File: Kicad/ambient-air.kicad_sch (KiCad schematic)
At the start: 38 parts, among them J1 USB_C_Receptacle_USB2.0_14P, J2 Conn_01x02, SW1 SW_Push, SW2 MINI MSK12CO2, SW3 SW_Push, U1 MCP73831T-2ACI/MC, U2 AP7361C-33SP-13, U3 ESP32-C3-WROOM-02, U4 TPD4E05U06DQA, U5 SHT4x, U6 STCC4-D1, U7 AHT20_C2757850, U8 SGP40-D-R4, U9 ICP-20100

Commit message: Separated PCBs
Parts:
- added C10: 4.7µF, Capacitor_SMD:C_0805_2012Metric, symbol Device:C_Small
- added J3, J4: Conn_01x04, Connector_JST:JST_SH_SM04B-SRSS-TB_1x04-1MP_P1.00mm_Horizontal, symbol Connector_Generic:Conn_01x04
- U7: now fitted
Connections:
- net +3V3: now also J3.1 (Pin_1); no longer C7.1, C8.1, C9.1, R6.2, U5.3 (VDD), U6.3 (ADDR), U6.6 (VDDIO), U6.7 (VDD), U7.2 (VDD), U8.5 (VDDH), U9.1 (CSB), U9.10 (VDDIO), U9.5 (VDD)
- net GND: now also J3.4 (Pin_4); no longer C7.2, C8.2, C9.2, U5.4 (VSS), U6.4 (VSS), U7.5 (GND), U8.2 (VSS), U8.4 (N/A), U8.7 (EXP), U9.3 (VSS), U9.6 (SDO/AD0), U9.8 (RESV), U9.9 (RESV)
- net SCL: now also J3.2 (Pin_2); no longer U6.1 (SCL), U7.3 (SCL), U8.6 (SCL), U9.2 (SCL)
- net SDA: now also J3.3 (Pin_3); no longer U6.5 (SDA), U7.4 (SDA), U8.3 (SDA), U9.4 (SDA/SDIO/SDI)
- new net +3V3_EXT: C10.1, C7.1, C8.1, C9.1, J4.1 (Pin_1), R6.2, U5.3 (VDD), U6.3 (ADDR), U6.6 (VDDIO), U6.7 (VDD), U7.2 (VDD), U8.5 (VDDH), U9.1 (CSB), U9.10 (VDDIO), U9.5 (VDD)
- new net GND_EXT: C10.2, C7.2, C8.2, C9.2, J4.4 (Pin_4), U5.4 (VSS), U6.4 (VSS), U7.5 (GND), U8.2 (VSS), U8.4 (N/A), U8.7 (EXP), U9.3 (VSS), U9.6 (SDO/AD0), U9.8 (RESV), U9.9 (RESV)
- new net SCL_EXT: J4.2 (Pin_2), U6.1 (SCL), U7.3 (SCL), U8.6 (SCL), U9.2 (SCL)
- new net SDA_EXT: J4.3 (Pin_3), U6.5 (SDA), U7.4 (SDA), U8.3 (SDA), U9.4 (SDA/SDIO/SDI)
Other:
- moved on the sheet: C7, C8, C9, J1, J2, JP1, R10, R6, R7, R8, R9, U5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

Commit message: Battery fuel gauge
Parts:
- added C11: 470nF, Capacitor_SMD:C_0805_2012Metric, symbol Device:C_Small
- added C12: 1µF, Capacitor_SMD:C_0805_2012Metric, symbol Device:C_Small
- added R11: 0.01Ω, Resistor_SMD:R_0805_2012Metric, symbol Device:R_Small
- added R12, R13: 10kΩ, Resistor_SMD:R_0805_2012Metric, symbol Device:R_Small
- added U10: BQ27441-G1, Package_SON:Texas_S-PDSO-N12, symbol Battery_Management:BQ27441-G1
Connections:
- net GND: now also C11.2, C12.1, R12.2, U10.13 (PAD), U10.3 (V_{SS})
- net SCL: now also U10.2 (SCL)
- net SDA: now also U10.1 (SDA)
- net VBAT: now also R11.1, U10.7 (SRN); no longer J2.1 (Pin_1)
- new net: R12.1, U10.10 (BIN)
- new net: R13.2, U10.12 (GPOUT)
- new net: C11.1, R13.1, U10.5 (V_{DD})
- new net VBAT_PRE: C12.2, J2.1 (Pin_1), R11.2, U10.6 (BAT), U10.8 (SRP)
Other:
- note added: "I2C Address: 0x55"
- moved on the sheet: C10, C7, C8, C9, J2, J4, R5, R6, U5, U6, U7, U8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

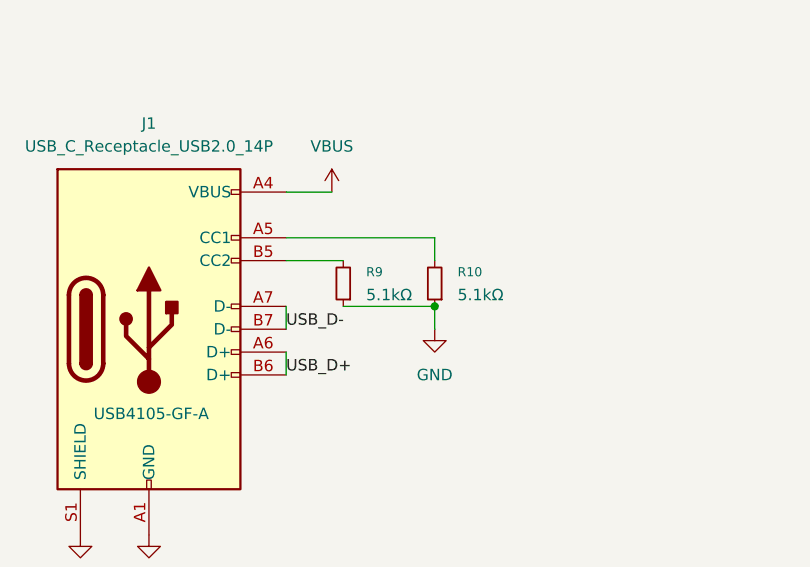
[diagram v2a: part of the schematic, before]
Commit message: Progress, saving data to storage
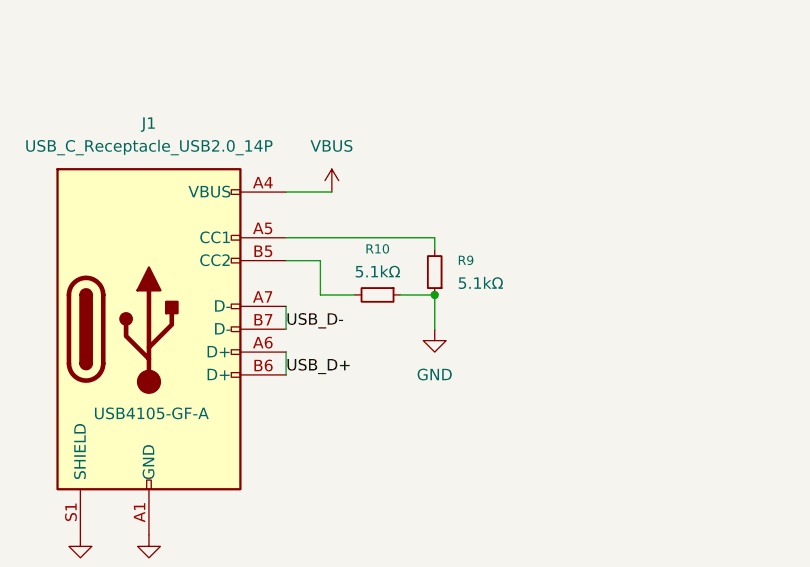
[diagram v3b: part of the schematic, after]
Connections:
- net at R10.2: now also J1.B5 (CC2); no longer J1.A5 (CC1)
- net at R9.2: now also J1.A5 (CC1); no longer J1.B5 (CC2)
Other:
- moved on the sheet: R10, R9
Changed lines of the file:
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@@
 	)
 	(junction
-		(at 162.56 165.1)
-		(diameter 0)
-		(color 0 0 0 0)
-	)
-	(junction
 		(at 142.24 115.57)
 		(diameter 0)
@@
 	)
 	(junction
+		(at 162.56 163.83)
+		(diameter 0)
+		(color 0 0 0 0)
+	)
+	(junction
 		(at 364.49 66.04)
 		(diameter 0)
@@
 	(wire
 		(pts
-			(xy 162.56 157.48) (xy 162.56 160.02)
-		)
-		(stroke
-			(width 0)
-			(type default)
-		)
-	)
-	(wire
-		(pts
 			(xy 142.24 115.57) (xy 143.51 115.57)
 		)
@@
 	(wire
 		(pts
+			(xy 162.56 163.83) (xy 162.56 167.64)
+		)
+		(stroke
+			(width 0)
+			(type default)
+		)
+	)
+	(wire
+		(pts
 			(xy 86.36 160.02) (xy 85.09 160.02)
 		)
@@
 	(wire
 		(pts
-			(xy 367.03 66.04) (xy 367.03 63.5)
+			(xy 162.56 157.48) (xy 162.56 158.75)
 		)
 		(stroke
@@
 	(wire
 		(pts
-			(xy 167.64 33.02) (xy 167.64 31.75)
+			(xy 367.03 66.04) (xy 367.03 63.5)
 		)
 		(stroke
@@
 	(wire
 		(pts
-			(xy 27.94 124.46) (xy 22.86 124.46)
+			(xy 167.64 33.02) (xy 167.64 31.75)
 		)
 		(stroke
@@
 	(wire
 		(pts
-			(xy 146.05 160.02) (xy 152.4 160.02)
+			(xy 27.94 124.46) (xy 22.86 124.46)
 		)
 		(stroke
@@
 	(wire
 		(pts
-			(xy 162.56 165.1) (xy 162.56 167.64)
+			(xy 314.96 148.59) (xy 321.31 148.59)
 		)
 		(stroke
@@
 	(wire
 		(pts
-			(xy 314.96 148.59) (xy 321.31 148.59)
+			(xy 119.38 77.47) (xy 123.19 77.47)
 		)
 		(stroke
@@
 	(wire
 		(pts
-			(xy 119.38 77.47) (xy 123.19 77.47)
+			(xy 38.1 21.59) (xy 81.28 21.59)
 		)
 		(stroke
@@
 	(wire
 		(pts
-			(xy 38.1 21.59) (xy 81.28 21.59)
+			(xy 146.05 160.02) (xy 149.86 160.02)
 		)
 		(stroke
@@
 	(wire
 		(pts
-			(xy 152.4 165.1) (xy 162.56 165.1)
-		)
-		(stroke
-			(width 0)
-			(type default)
-		)
-	)
-	(wire
-		(pts
 			(xy 334.01 144.78) (xy 317.5 144.78)
 		)
@@
 	(wire
 		(pts
+			(xy 149.86 160.02) (xy 149.86 163.83)
+		)
+		(stroke
+			(width 0)
+			(type default)
+		)
+	)
+	(wire
+		(pts
 			(xy 344.17 157.48) (xy 344.17 158.75)
 		)
@@
 	(wire
 		(pts
+			(xy 158.75 163.83) (xy 162.56 163.83)
+		)
+		(stroke
+			(width 0)
+			(type default)
+		)
+	)
+	(wire
+		(pts
 			(xy 52.07 48.26) (xy 64.77 48.26)
 		)
@@
 	(wire
 		(pts
+			(xy 149.86 163.83) (xy 153.67 163.83)
+		)
+		(stroke
+			(width 0)
+			(type default)
+		)
+	)
+	(wire
+		(pts
 			(xy 50.8 76.2) (xy 71.12 76.2)
 		)
@@
 	(symbol
 		(lib_id "Device:R_Small")
-		(at 162.56 162.56 180)
+		(at 156.21 163.83 270)
 		(unit 1)
 		(exclude_from_sim no)
@@
 		(fields_autoplaced yes)
 		(property "Reference" "R10"
-			(at 165.1 161.2899 0)
+			(at 156.21 158.75 90)
 			(effects
 				(font
 					(size 1.016 1.016)
 				)
-				(justify right)
 			)
 		)
 		(property "Value" "5.1kΩ"
-			(at 165.1 163.8299 0)
+			(at 156.21 161.29 90)
 			(effects
 				(font
 					(size 1.27 1.27)
 				)
-				(justify right)
 			)
 		)
 		(property "Footprint" "Resistor_SMD:R_0805_2012Metric"
-			(at 162.56 162.56 0)
+			(at 156.21 163.83 0)
 			(effects
 				(font
@@
 		)
 		(property "Datasheet" "~"
-			(at 162.56 162.56 0)
+			(at 156.21 163.83 0)
 			(effects
 				(font
@@
 		)
 		(property "Description" "Resistor, small symbol"
-			(at 162.56 162.56 0)
+			(at 156.21 163.83 0)
 			(effects
 				(font
@@
 	(symbol
 		(lib_id "Device:R_Small")
-		(at 152.4 162.56 180)
+		(at 162.56 161.29 180)
 		(unit 1)
 		(exclude_from_sim no)
@@
 		(fields_autoplaced yes)
 		(property "Reference" "R9"
-			(at 154.94 161.2899 0)
+			(at 165.1 160.0199 0)
 			(effects
 				(font
@@
 		)
 		(property "Value" "5.1kΩ"
-			(at 154.94 163.8299 0)
+			(at 165.1 162.5599 0)
 			(effects
 				(font
@@
 		)
 		(property "Footprint" "Resistor_SMD:R_0805_2012Metric"
-			(at 152.4 162.56 0)
+			(at 162.56 161.29 0)
 			(effects
 				(font
@@
 		)
 		(property "Datasheet" "~"
-			(at 152.4 162.56 0)
+			(at 162.56 161.29 0)
 			(effects
 				(font
@@
 		)
 		(property "Description" "Resistor, small symbol"
-			(at 152.4 162.56 0)
+			(at 162.56 161.29 0)
 			(effects
 				(font

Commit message: Progress
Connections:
- net at R1.2, U3.2 (EN/CHIP_PU): no longer SW1.2
- net at U3.3 (GPIO4/ADC1_CH4): now also SW1.2
- no-connect marks 23 -> 22
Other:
- moved on the sheet: R4, SW1, SW3

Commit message: Get basic sampling working
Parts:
- removed JP1: Jumper_2_Open, Jumper:SolderJumper-2_P1.3mm_Open_TrianglePad1.0x1.5mm, symbol Jumper:Jumper_2_Open
- removed R7: 12kΩ, Resistor_SMD:R_0603_1608Metric, symbol Device:R_Small
- removed R8: 10kΩ, Resistor_SMD:R_0603_1608Metric, symbol Device:R_Small
- added R16: 668kΩ, Resistor_SMD:R_0603_1608Metric, symbol Device:R_Small
- added R17: 220kΩ, Resistor_SMD:R_0603_1608Metric, symbol Device:R_Small
- added U11: TPS2116DRL, Package_TO_SOT_SMD:SOT-583-8, symbol Power_Management:TPS2116DRL
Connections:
- net GND: now also R17.2, U11.1 (GND)
- net VBAT: now also U11.6 (VIN2); no longer C1.1, SW2.3, U2.8 (IN)
- net VBUS: now also R16.2, U11.3 (VIN1), U11.5 (MODE)
- net VBAT_DIV renamed PWR_SRC
- net PWR_SRC: now also U11.8 (ST)
- new net: R16.1, R17.1, U11.4 (PR1)
- new net VDEV: C1.1, SW2.3, U11.2 (VOUT), U11.7 (VOUT), U2.8 (IN)
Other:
- note added: "MODE = VIN1 = Automode/Priority"
- note added: "Ratio of 0.23 = switch at 4.6V"
- moved on the sheet: R1
